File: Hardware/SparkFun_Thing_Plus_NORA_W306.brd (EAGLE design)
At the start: 22.9 x 58.4 mm, 152 parts, among them J1 THING_PLUS_LOGICAL, J2 LiPo, J3 QWIIC_RA, J4 MICRO-SDFRICTION, J5 USB-C, J6 SWD (DNP), Q1 3.1A/30V/105mΩ, Q2 MBT3904DW1T1, U1 UBLOX_NORA_W306, U3 XC6222B331MR-G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

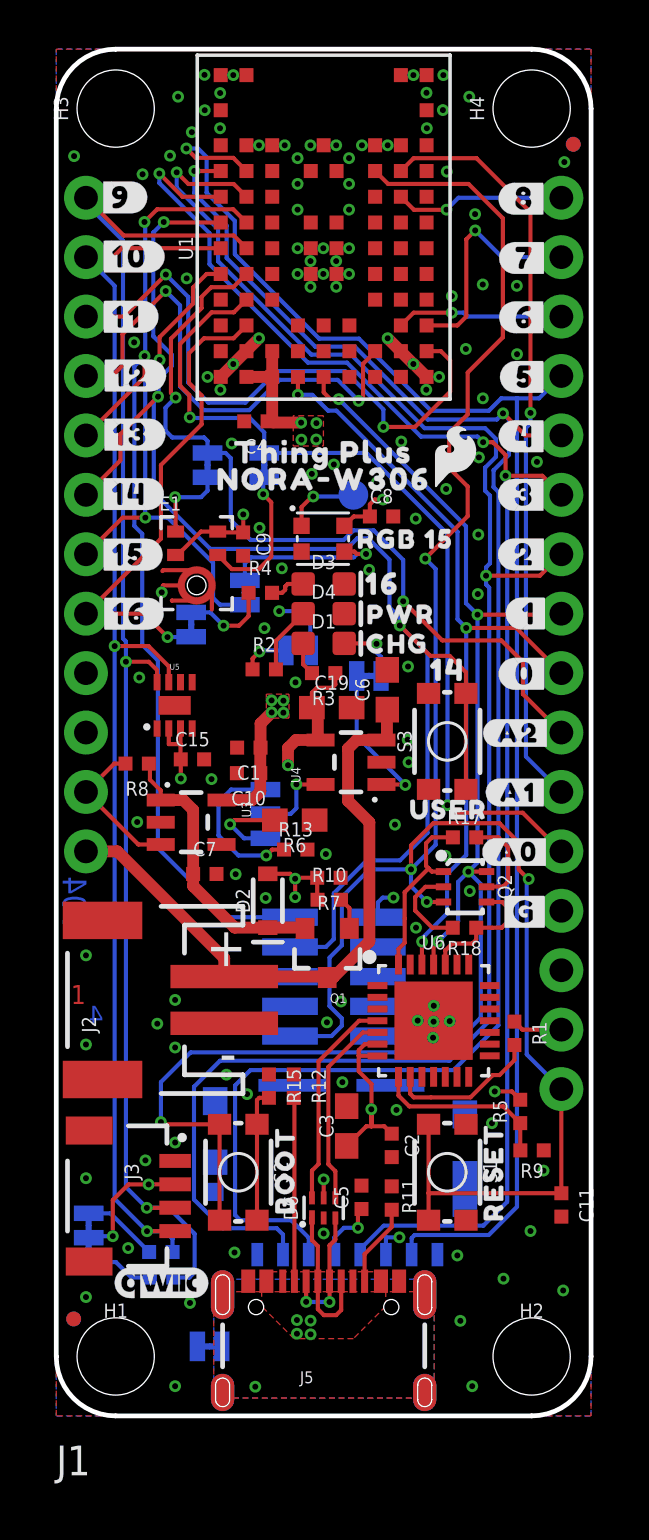
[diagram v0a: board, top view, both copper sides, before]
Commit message: Correcting SWD_DATA and SWD_CLK
-In the Symbol Pin names, Removed SWD DATA and CL from PB18/PB19
-Removed PDM mic
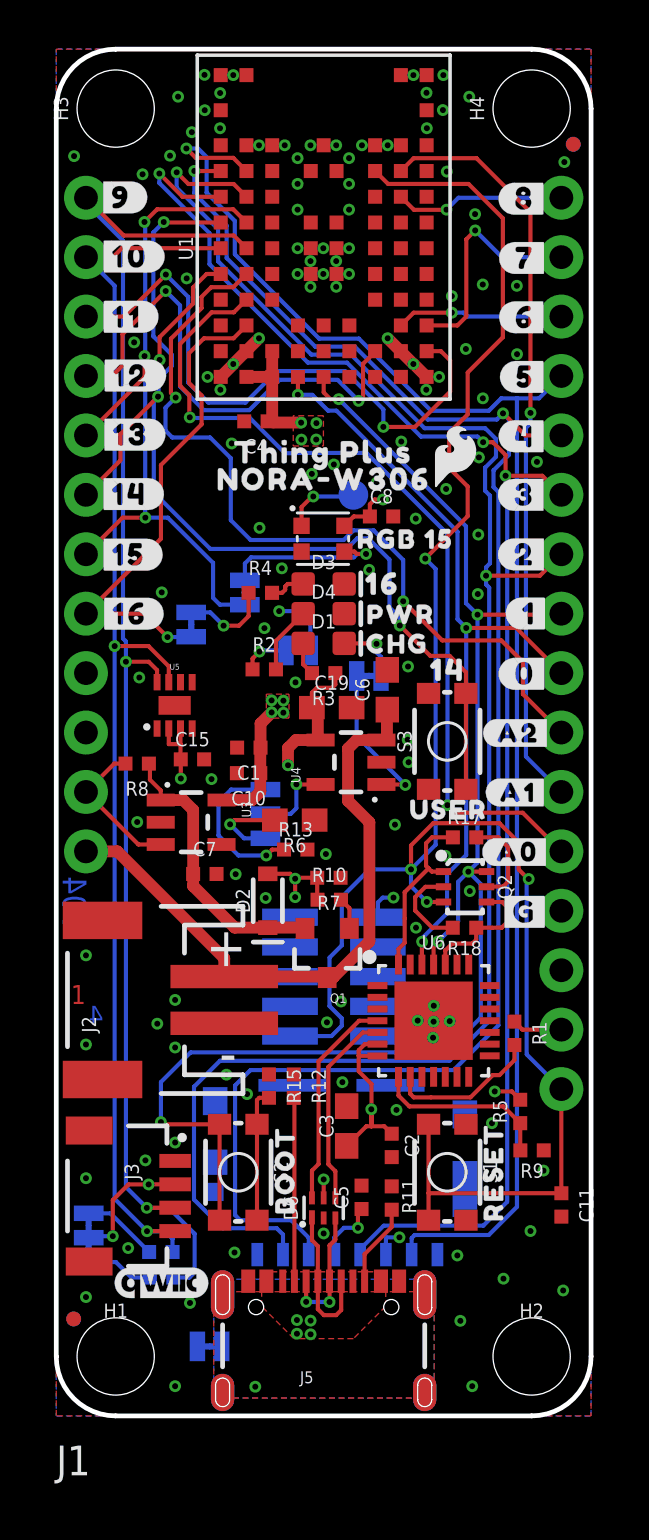
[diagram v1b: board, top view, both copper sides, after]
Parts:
- removed C9: 0.1uF, SparkFun-Capacitors:0402-TIGHT
- removed E1: SPH0641LM4H-1, SparkFun-Sensors:SPH0641LM4H-1_MICROPHONE
- removed JP1, JP2: (no value), SparkFun-Jumpers:SMT-JUMPER_2_NC_TRACE_SILK
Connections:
- removed net N$29: E1.1, JP2.1
- removed net N$30: E1.4, JP1.1
- removed net PA27: J1.13, U1.H2
- removed net PB1/ADC/DMIC_CLK: J1.24, JP1.2, U1.D8
- removed net PB18/SWD_CL: J1.6, J6.4, S3.1, S3.2, U1.G9
- removed net PB19/SWD_DATA: J1.5, J6.2, U1.G8
- removed net PB2/DMIC_DATA: J1.22, JP2.2, U1.E8
- removed net PB3/ADC: J1.23, U1.J2
- new net PA27/SWD_DATA: J1.13, J6.2, U1.H2
- new net PB1: J1.24, U1.D8
- new net PB18: J1.6, S3.1, S3.2, U1.G9
- new net PB19: J1.5, U1.G8
- new net PB2: J1.22, U1.E8
- new net PB3/ADC/SWD_CLK: J1.23, J6.4, U1.J2
- net 3.3V: no longer C9.1, E1.2, E1.5
- net GND: no longer C9.2, E1.3, E1.6, E1.7, E1.8
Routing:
- net PB18/SWD_CL: track 62.0 -> 0.00 mm, vias 3 -> 0
- net PB18: track 0.00 -> 43.6 mm, vias 0 -> 3
- net PB19/SWD_DATA: track 43.5 -> 0.00 mm, vias 2 -> 0
- net PB1/ADC/DMIC_CLK: track 37.8 -> 0.00 mm, vias 2 -> 0
- net PB1: track 0.00 -> 37.3 mm, vias 0 -> 2
- net PB2/DMIC_DATA: track 35.1 -> 0.00 mm, vias 2 -> 0
- net PB2: track 0.00 -> 34.8 mm, vias 0 -> 2
- net PB3/ADC/SWD_CLK: track 0.00 -> 32.2 mm, vias 0 -> 1
- net PB3/ADC: track 32.2 -> 0.00 mm, vias 1 -> 0
- net PB19: track 0.00 -> 15.0 mm, vias 0 -> 2
- net PA27/SWD_DATA: track 0.00 -> 7.31 mm, vias 0 -> 1
- net PA27: track 7.31 -> 0.00 mm, vias 1 -> 0
- net N$30: track 6.31 -> 0.00 mm, vias 1 -> 0
- net GND: track 10.4 -> 6.02 mm
- net 3.3V: track 49.8 -> 45.7 mm, vias 16 -> 15
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
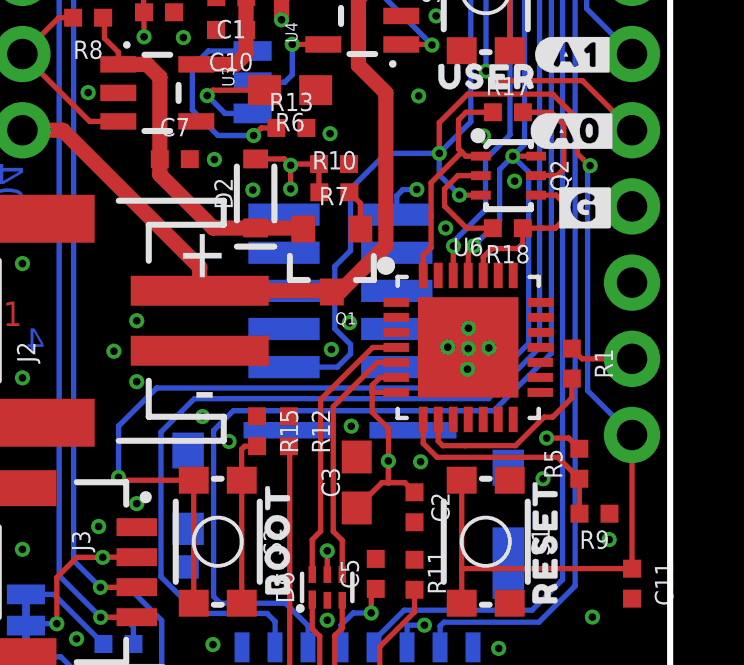
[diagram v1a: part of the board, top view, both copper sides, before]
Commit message: Switched CP2102 to QFN24 package type
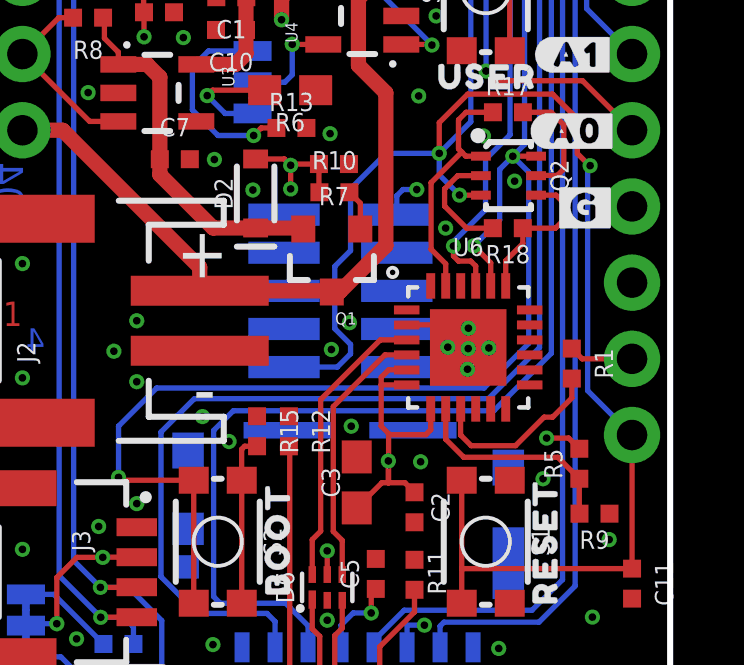
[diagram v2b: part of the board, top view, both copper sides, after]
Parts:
- U6: value CP2102N_QFN28 -> CP2102N; device nora-w306:QFN28 -> SparkFun-IC-Comms:QFN24
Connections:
- net 3.3V: now also U6.5
- net DTR: now also U6.23; no longer U6.28
- net GND: now also U6.2, U6.PAD; no longer U6.3
- net N$15: now also U6.3; no longer U6.4
- net N$18: now also U6.4; no longer U6.5
- net PA7/UART-LOG-TXD: now also U6.20; no longer U6.25
- net PA8/UART-LOG-RXD: now also U6.21; no longer U6.26
- net RTS: now also U6.19; no longer U6.24
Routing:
- net 3.3V: track 45.7 -> 48.1 mm
- net GND: track 6.02 -> 7.53 mm
- net PA8/UART-LOG-RXD: track 34.3 -> 35.2 mm
- net N$1: track 6.55 -> 6.03 mm
- net PA7/UART-LOG-TXD: track 62.8 -> 63.4 mm

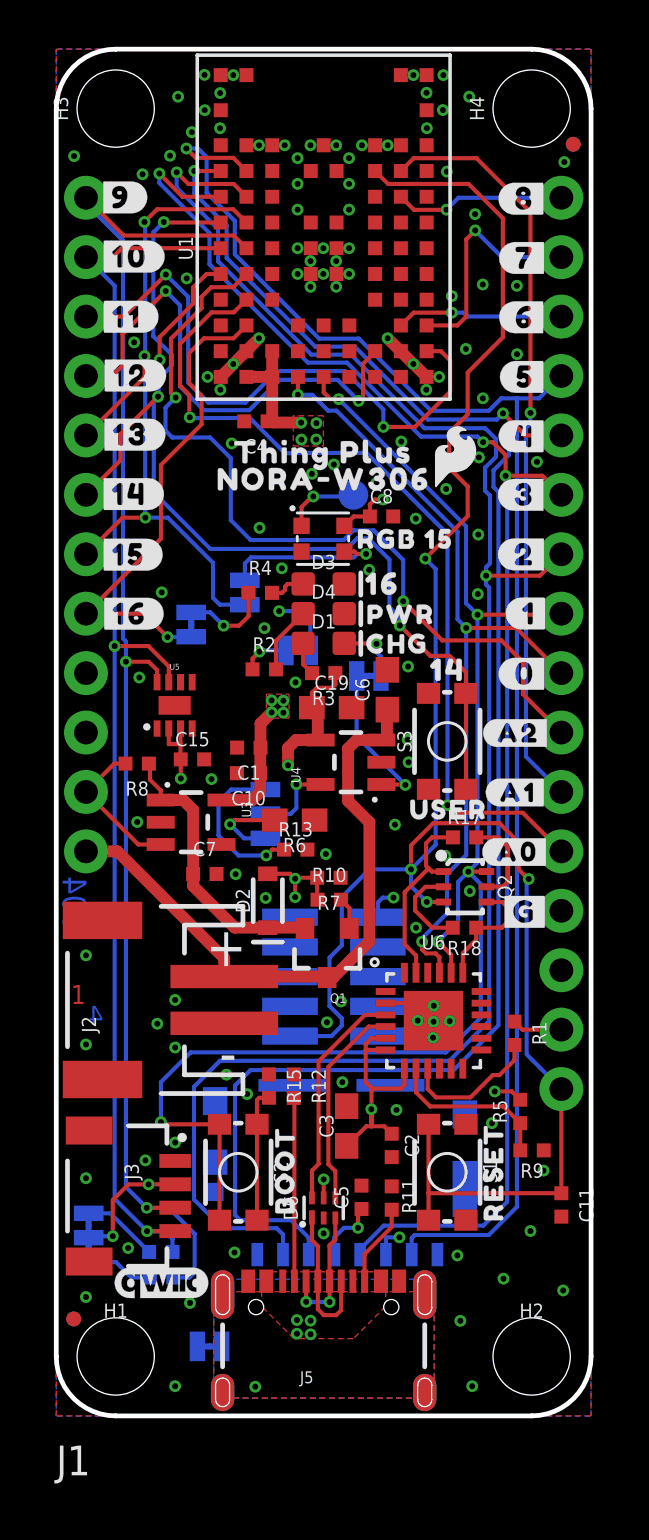
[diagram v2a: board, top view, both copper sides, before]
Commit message: Rerouted with new pin selections
-SPI0 now used for "main" SPI headers and uSD
-SPI1 PICO pin used for WS2812 control
-RX1/TX1 pins changed to other option on module
-I2C pins changed to other option on module
-SWD lines routed to DNP header on bottom side.
-most GPIOs switched/rerouted *note, Arduino pin map table not yet updated*
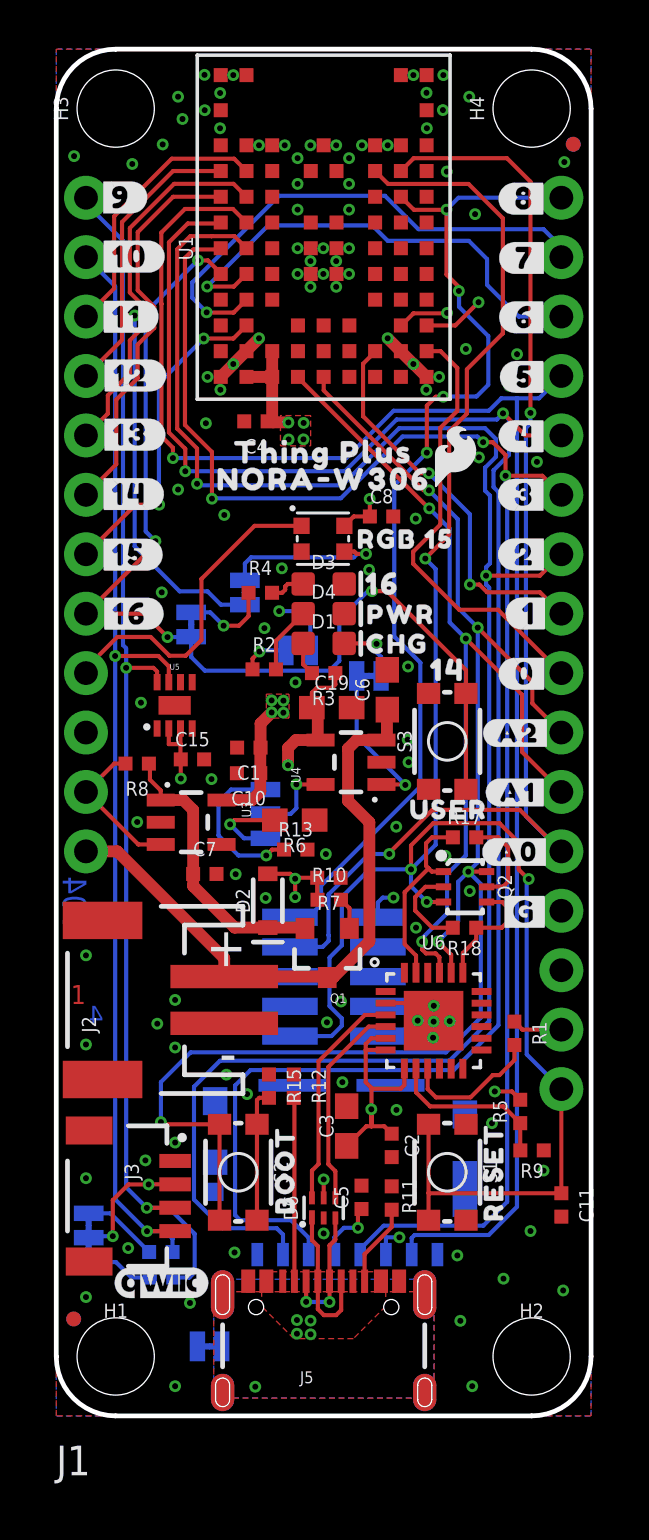
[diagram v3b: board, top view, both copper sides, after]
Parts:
- removed TP2: TEST-POINT3X5, SparkFun-Connectors:PAD.03X.05
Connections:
- removed net N$28: D5.DO, TP2.1
- removed net PA12/PICO: J1.17, J4.3, U1.J9
- removed net PA13/POCI: J1.16, J4.7, U1.J8
- removed net PA14/SCK: J1.18, J4.5, U1.H9
- removed net PA15/CS: J1.19, J4.2, U1.H8
- removed net PA25/LP_UART_RXD: J1.15, U1.C2
- removed net PA26/LP_UART_TXD: J1.14, U1.C1
- removed net PB1: J1.24, U1.D8
- removed net PB18: J1.6, S3.1, S3.2, U1.G9
- removed net PB19: J1.5, U1.G8
- removed net PB2: J1.22, U1.E8
- removed net PB20/SCL: J1.2, J3.4, R28.1, U1.F9, U5.7
- removed net PB21/SDA: J1.1, J3.3, R29.1, U1.F8, U5.8
- removed net PB3/ADC/SWD_CLK: J1.23, J6.4, U1.J2
- new net PA12: J1.4, JP3.1, U1.J9
- new net PA13: J1.3, U1.J8
- new net PA14: J1.6, U1.H9
- new net PA15: J1.5, U1.H8
- new net PA25/SCL: J1.2, J3.4, R28.1, U1.C2, U5.7
- new net PA26/SDA: J1.1, J3.3, R29.1, U1.C1, U5.8
- new net PB1/LP_UART_TXD/A2: J1.14, U1.D8
- new net PB18/SPI0_PICO: J1.17, J4.3, U1.G9
- new net PB19/SPI0_POCI: J1.16, J4.7, U1.G8
- new net PB2/LP_UART_RXD/A1: J1.15, U1.E8
- new net PB20/SPI0_CLK: J1.18, J4.5, U1.F9
- new net PB21/SPI0_CS: J1.19, J4.2, U1.F8
- new net PB3/SWD_CLK/A0: J1.24, J6.4, U1.J2
- new net WS2812-DO: D5.DO, J1.9
- net PA28: now also J1.20; no longer J1.4
- net PA30: now also J1.21; no longer J1.3
- net PA7/UART-LOG-TXD: now also J1.22; no longer J1.20
- net PA8/UART-LOG-RXD: now also J1.23; no longer J1.21
- net PB22: now also J1.8, JP4.1, S3.1, S3.2; no longer J1.7, JP3.1
- net PB23: now also J1.7; no longer J1.8, JP4.1
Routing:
- net PB21/SPI0_CS: track 0.00 -> 80.6 mm, vias 0 -> 2
- net PB18/SPI0_PICO: track 0.00 -> 78.9 mm, vias 0 -> 2
- net PA15/CS: track 75.7 -> 0.00 mm, vias 2 -> 0
- net PA26/SDA: track 0.00 -> 74.7 mm, vias 0 -> 3
- net PB19/SPI0_POCI: track 0.00 -> 72.5 mm, vias 0 -> 1
- net PA12/PICO: track 71.8 -> 0.00 mm, vias 2 -> 0
- net PB20/SPI0_CLK: track 0.00 -> 68.5 mm, vias 0 -> 3
- net PA25/SCL: track 0.00 -> 67.9 mm, vias 0 -> 3
- net PA13/POCI: track 66.3 -> 0.00 mm, vias 1 -> 0
- net PA14/SCK: track 65.9 -> 0.00 mm, vias 3 -> 0
- net PB21/SDA: track 60.4 -> 0.00 mm, vias 2 -> 0
- net PB20/SCL: track 55.0 -> 0.00 mm, vias 2 -> 0
- net PB3/SWD_CLK/A0: track 0.00 -> 51.5 mm, vias 0 -> 2
- net PB18: track 43.6 -> 0.00 mm, vias 3 -> 0
- net PB1: track 37.3 -> 0.00 mm, vias 2 -> 0
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
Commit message: Silk Labels updated
-and some minor layout tweaks
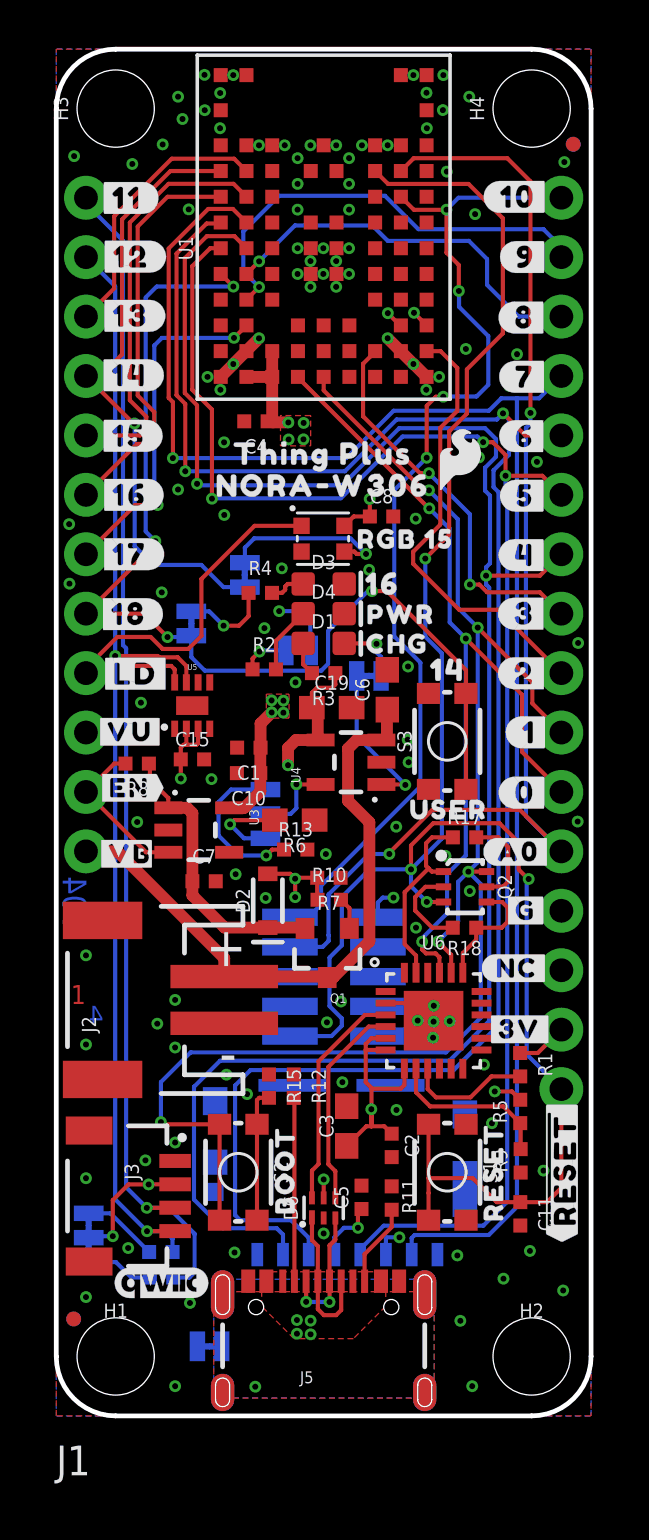
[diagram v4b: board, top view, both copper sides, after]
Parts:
- removed JP3, JP4: (no value), SparkFun-Jumpers:SMT-JUMPER_2_NC_TRACE_SILK
- removed U$21: (no value), output:#6#RX1#6
- removed U$22: (no value), output:#7#TX1#7
- removed U$24: (no value), output:#8#8
- removed U$26: (no value), output:#SDA#9#10
- removed U$27: (no value), output:#SCL#10#10
- removed U$28: (no value), output:#11#11
- removed U$29: (no value), output:#12#12
- added JP1, JP2: (no value), SparkFun-Jumpers:SMT-JUMPER_2_NC_TRACE_SILK
- added U$75: (no value), output:#G#22
- added U$76: (no value), output:#VU#23
- added U$77: (no value), output:#VB26
- added U$80: (no value), output:#EN#27
- added U$81: (no value), output:#2#28
- added U$82: (no value), output:#3#28
- added U$83: (no value), output:#4#CS#28
- added U$84: (no value), output:#5#SCK#28
- added U$85: (no value), output:#6#PICO#28
- added U$86: (no value), output:#7#POCI#28
- added U$87: (no value), output:#9#TX1#A2#28
- added U$88: (no value), output:#8#RX1#A1#28
- added U$91: (no value), output:#10#28
- U$1: device output:#9#91420 -> output:#17#11
- U$13: device output:#A1#1 -> output:#SDA#11#28
- U$14: device output:#A2#4 -> output:#17#28
- U$17: device output:#3#SCK#5 -> output:#SCL#12#28
- U$18: device output:#4#PICO#5 -> output:#18#28
- U$19: device output:#5#POCI#5 -> SparkFun-Aesthetics:SFE_LOGO_FLAME_.1
- U$20: device output:#2#CS#5 -> output:#LD#29
- U$35: device output:#10#91420 -> output:#18#18
- U$57: device output:#G#18 -> output:#3V#23
- U$58: device output:#JP3#0 -> output:#JP2#0
- U$65: device output:#NC#1 -> output:#JP1#0
- U$68: device output:#A1#18 -> output:##RESET##19
- U$69: device output:#A2#18 -> output:#NC#21
- U$70: device output:#JP1#18 -> output:#9#10
- U$71: device output:#JP2#18 -> output:#LED_DO#0
- U$74: device output:#JP4#0 -> output:#10#11
- moved LOGO3 38.6 mm to (4.54, 16.3), turned to 270 degrees
- moved U$13 29.3 mm to (5.00, 52.1)
- moved U$74 24.9 mm to (19.7, 52.1), flipped to the top, turned to 0 degrees
- moved LOGO2 24.1 mm to (11.4, 43.2)
- moved U$14 18.0 mm to (3.15, 36.8)
- moved U$17 16.6 mm to (5.02, 49.6)
- moved U$18 16.6 mm to (3.11, 34.3)
- moved U$68 16.2 mm to (21.6, 10.5), turned to 90 degrees
- moved U$20 16.1 mm to (3.38, 31.7), flipped to the top
- moved U$70 16.0 mm to (20.1, 49.5), flipped to the top, turned to 0 degrees
- moved U$35 15.3 mm to (3.11, 34.3)
- moved U$1 15.3 mm to (3.16, 36.8)
- moved U$19 14.0 mm to (7.59, 54.0)
- moved U$69 10.1 mm to (19.7, 19.1)
- moved U$10 8.81 mm to (12.4, 56.2)
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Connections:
- net N$10: now also JP1.2; no longer JP3.2
- net N$22: now also JP2.2; no longer JP4.2
- net PA12: now also JP1.1; no longer JP3.1
- net PB22: now also JP2.1; no longer JP4.1
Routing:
- net PB2/LP_UART_RXD/A1: track 20.4 -> 16.6 mm
- net PA26/SDA: track 74.7 -> 71.2 mm
- net PA25/SCL: track 67.9 -> 64.7 mm
- net PB1/LP_UART_TXD/A2: track 22.1 -> 19.0 mm
- net PA12: track 28.5 -> 26.4 mm
- net PA15: track 16.2 -> 17.7 mm
- net PB23: track 14.0 -> 15.1 mm
- net PB19/SPI0_POCI: track 72.5 -> 71.7 mm
- net PB22: track 45.4 -> 46.2 mm
- net PB18/SPI0_PICO: track 78.9 -> 78.1 mm
- net PB21/SPI0_CS: track 80.6 -> 79.9 mm
- net N$1: track 6.03 -> 5.35 mm
- net !RESET!: track 82.3 -> 82.9 mm
- net PB20/SPI0_CLK: track 68.5 -> 67.8 mm
- net GND: vias 111 -> 117
